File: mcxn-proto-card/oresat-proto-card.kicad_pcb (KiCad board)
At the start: 4 copper layers, 99.8 x 94.6 mm, 128 parts, among them J1 J-SAMTEC-TFM-110-01-L-D-RA, J2 U.FL, J3 U.FL, J4 U.FL, J6 J-SAMTEC-TFM-120-X1-XXX-D-RA, J7 ORESAT-DEBUG-CONNECTOR-ALL, Q1 DMP2240UDM, Q2 DMP3050LVT-7, Q7 MOSFET-PCH-SOT23-6, Q8 PMV45EN, Q9 PMV45EN, U1 TCAN330, U10 TPS62111RSA, U11 MIC842LYC5, U12 MIC842LYC5, U2 MAX7310, U3 TS5A21366DCUR, U6 MAX4211, U7 STM32F091C, X2 CRYSTAL-WITH-GND

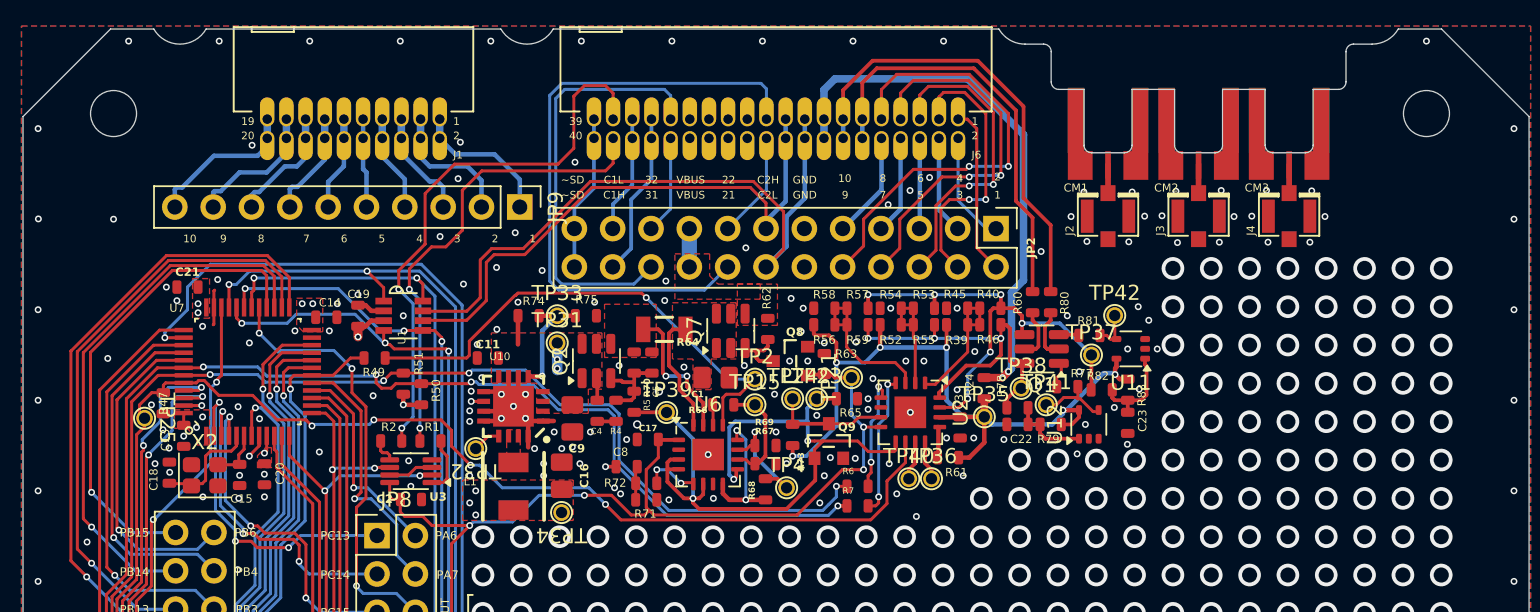
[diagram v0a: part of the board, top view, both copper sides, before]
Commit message: Eagle libraries replaced, scheatic and layout clean up cont.
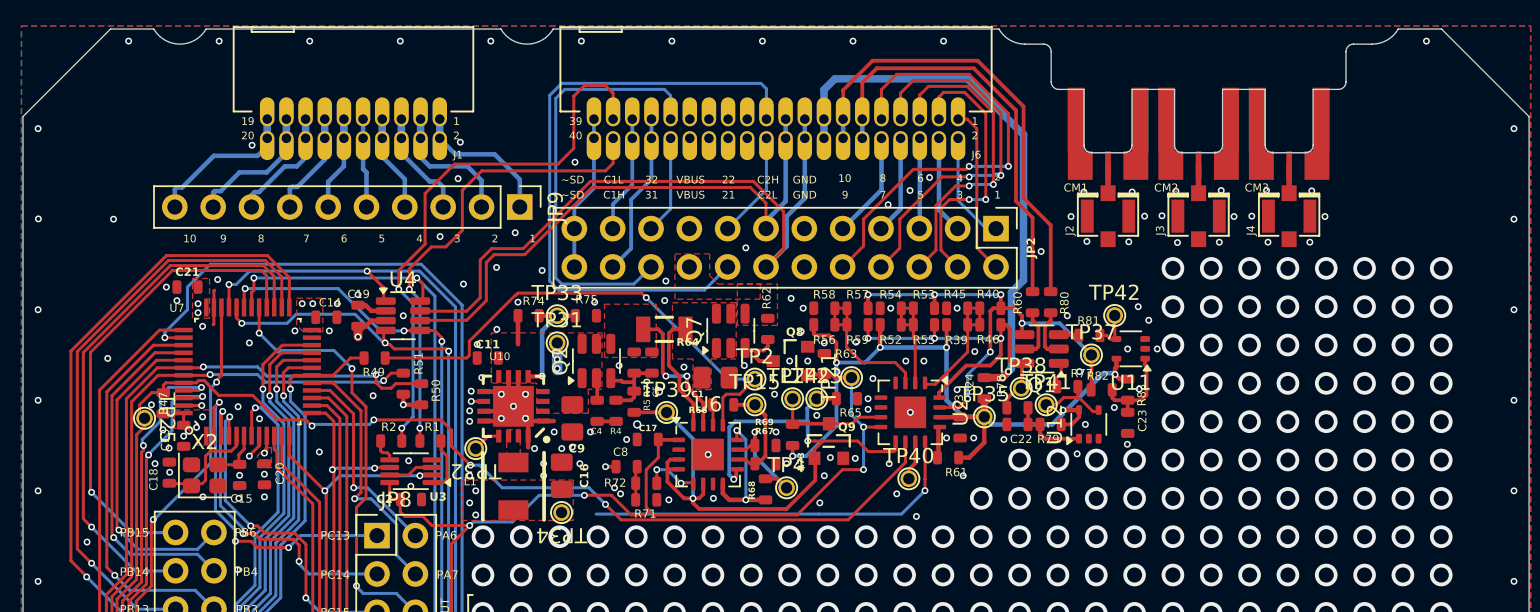
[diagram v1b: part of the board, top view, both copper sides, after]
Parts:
- removed H2, H3: STAND-OFFTIGHT, oresat-proto-card:STAND-OFF-TIGHT
- removed R6, R7: 0, oresat-passives:0603-C-NOSILK
- removed TP36: Test-Point, oresat-misc:TestPoint-0.75mm-th
- removed U1: TCAN330, oresat-ics:SOT23-8_TI-DCN
- added U4: TCAN330, Package_TO_SOT_SMD:SOT-23-8, F.Cu at (123.8, 76.7)
- J7: footprint oresat-connectors:J-TE-2-1734592-0 -> oresat-proto-card:TE_2-1734592-0
- R75: value NP -> 10k
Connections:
- JP2 pad 1: /Connectors/SPARE2 -> /Connectors/SPARE10
- JP2 pad 10: /Connectors/SPARE9 -> VBUS
- JP2 pad 11: GND -> /Connectors/SPARE5
- JP2 pad 12: GND -> /Connectors/SPARE31
- JP2 pad 13: CAN2_L -> /Connectors/SPARE4
- JP2 pad 14: CAN2_H -> /Connectors/SPARE32
- JP2 pad 15: /Connectors/SPARE22 -> /Connectors/SPARE3
- JP2 pad 16: /Connectors/SPARE21 -> /Connectors/CAN1_H
- JP2 pad 17: VBUS -> /Connectors/SPARE2
- JP2 pad 18: VBUS -> /Connectors/CAN1_L
- JP2 pad 19: /Connectors/SPARE32 -> /Connectors/SPARE1
- JP2 pad 2: /Connectors/SPARE1 -> CAN2_H
- JP2 pad 20: /Connectors/SPARE31 -> /Connectors/~{SD}
- JP2 pad 21: /Connectors/CAN1_L -> GND
- JP2 pad 22: /Connectors/CAN1_H -> GND
- JP2 pad 23: /Connectors/~{SD} -> (no net)
- JP2 pad 24: /Connectors/~{SD} -> (no net)
- JP2 pad 3: /Connectors/SPARE4 -> /Connectors/SPARE9
- JP2 pad 4: /Connectors/SPARE3 -> CAN2_L
- JP2 pad 5: /Connectors/SPARE6 -> /Connectors/SPARE8
- JP2 pad 6: /Connectors/SPARE5 -> /Connectors/SPARE21
- JP2 pad 7: /Connectors/SPARE8 -> /Connectors/SPARE7
- JP2 pad 8: /Connectors/SPARE7 -> /Connectors/SPARE22
- JP2 pad 9: /Connectors/SPARE10 -> /Connectors/SPARE6
- Q9 pad 1: /Power/CB-RESET -> /Power/CB_CTRL
- R5 pad 1: /Power/CB-RESET -> /Power/CB_CTRL
- TP39 pad 1: /Power/CB-RESET -> /Power/CB_CTRL
- U2 pad 12: Net-(U2-IO7) -> /Power/UART_EN
- U3 pad 3: Net-(U3-IN1) -> /Power/UART_EN
- U3 pad 7: Net-(U3-IN1) -> /Power/UART_EN
- U6 pad 3: /Power/CB-RESET -> /Power/CB_CTRL
- U6 pad 4: /Power/CB-RESET -> /Power/CB_CTRL
- U6 pad 6: /Power/CB-RESET -> /Power/CB_CTRL
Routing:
- net PB7/SDA: track 88.8 -> 52.6 mm, vias 5 -> 3
- net PB6/SCL: track 91.3 -> 57.3 mm, vias 4 -> 2
- net /Power/UART_EN: track 0.00 -> 28.8 mm, vias 0 -> 1
- net Net-(U2-IO0): track 9.42 -> 0.00 mm, vias 2 -> 0
- net Net-(U2-IO1): track 7.71 -> 0.00 mm, vias 2 -> 0
- net Net-(U3-IN1): track 3.16 -> 0.00 mm
- net Net-(U2-IO7): track 2.72 -> 0.00 mm
- net VBUS: track 2.54 -> 0.00 mm
- net BOOT0: track 95.6 -> 94.7 mm

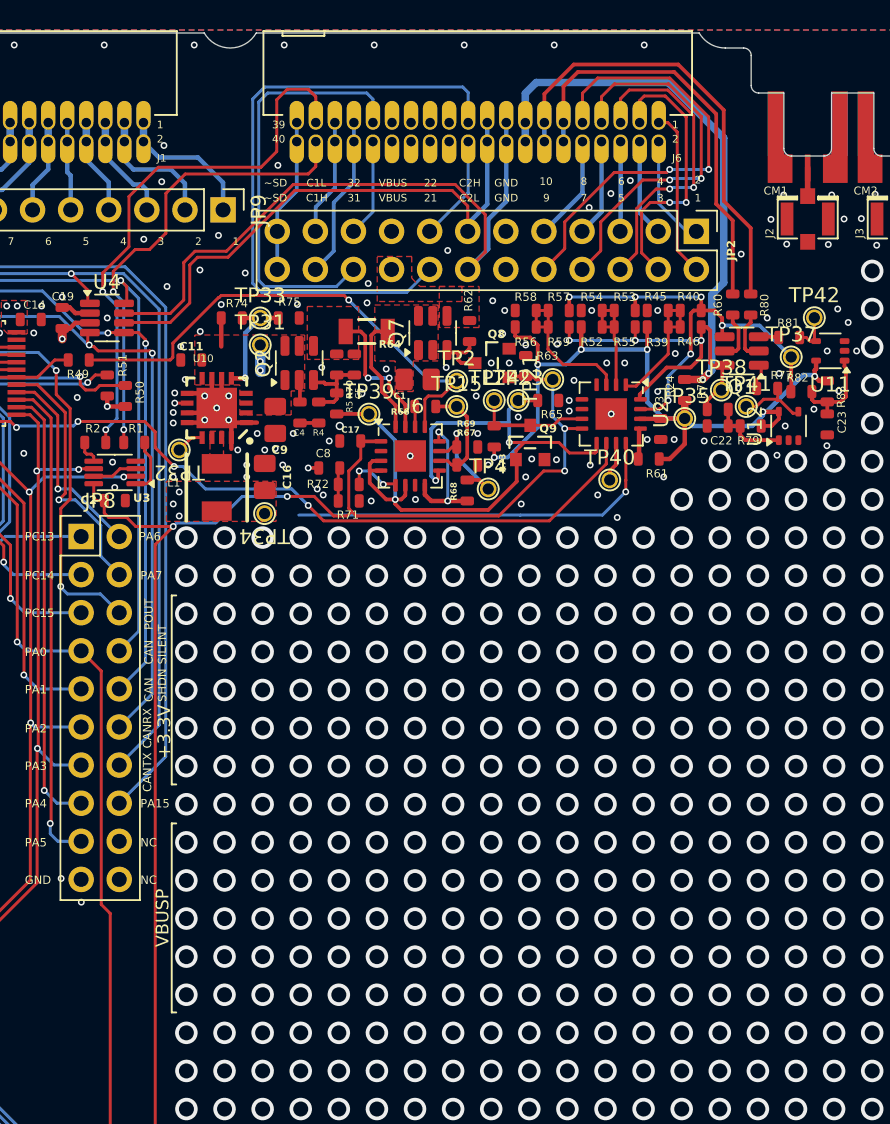
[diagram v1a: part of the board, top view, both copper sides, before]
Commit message: Cleaned up layout and routing
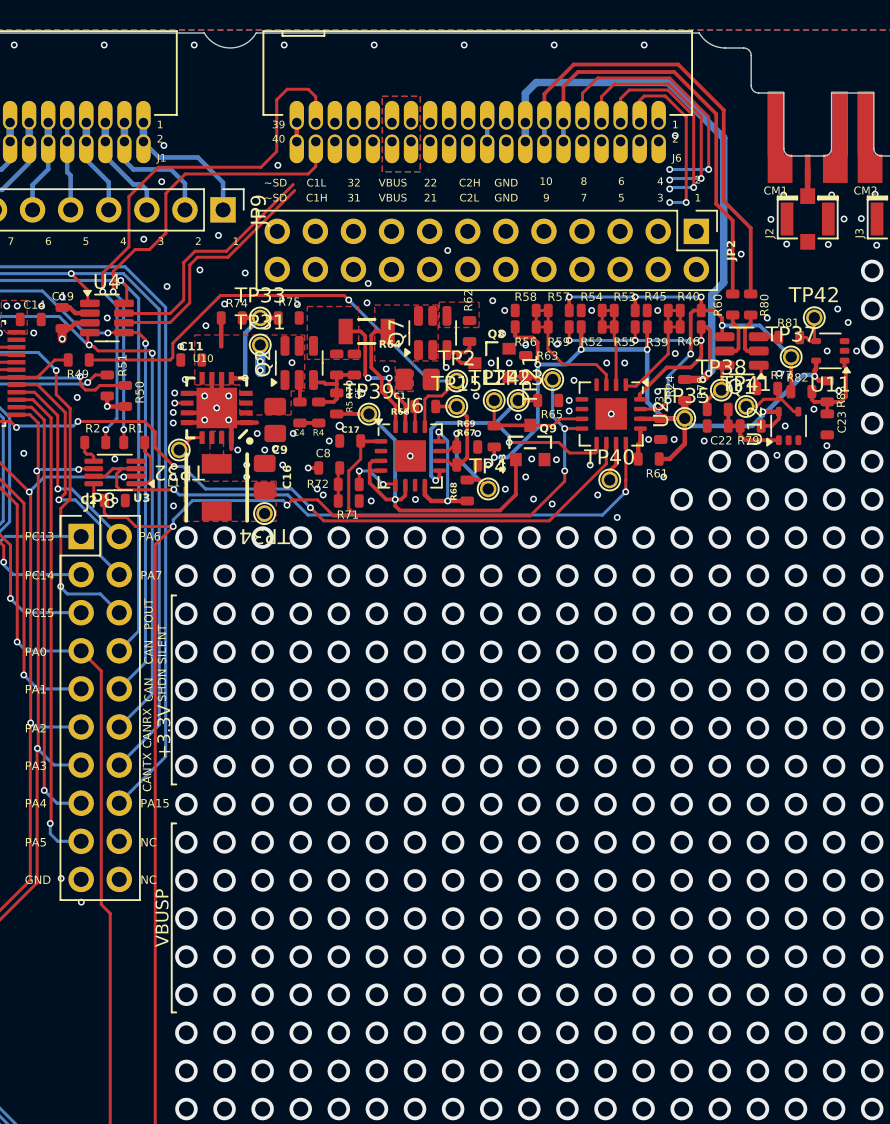
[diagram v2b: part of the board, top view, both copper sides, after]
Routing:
- net /Connectors/SPARE21: track 41.8 -> 0.00 mm
- net CAN2_H: track 44.8 -> 16.1 mm
- net /Connectors/SPARE31: track 28.4 -> 0.00 mm
- net /Power/CB-RESET: track 48.4 -> 20.7 mm, vias 3 -> 2
- net /Power/CB_CTRL: track 0.00 -> 26.7 mm, vias 0 -> 1
- net CAN2_L: track 37.8 -> 17.6 mm
- net GND: track 23.9 -> 43.0 mm, vias 312 -> 323
- net VBUSP: track 39.1 -> 20.0 mm, vias 12 -> 7
- net /Power/UART_EN: track 28.8 -> 43.1 mm, vias 1 -> 2
- net /Connectors/SPARE9: track 30.2 -> 18.0 mm
- net /Connectors/CAN1_H: track 11.2 -> 0.00 mm
- net /Connectors/SPARE1: track 11.2 -> 0.00 mm
- net /Connectors/SPARE7: track 25.3 -> 15.9 mm
- net /Connectors/~{SD}: track 10.3 -> 1.27 mm
- net /Connectors/CAN1_L: track 7.79 -> 0.00 mm
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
